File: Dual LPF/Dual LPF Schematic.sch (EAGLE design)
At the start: 84 parts, among them U1 TL074_, U2 TL074_, U3 TL074_

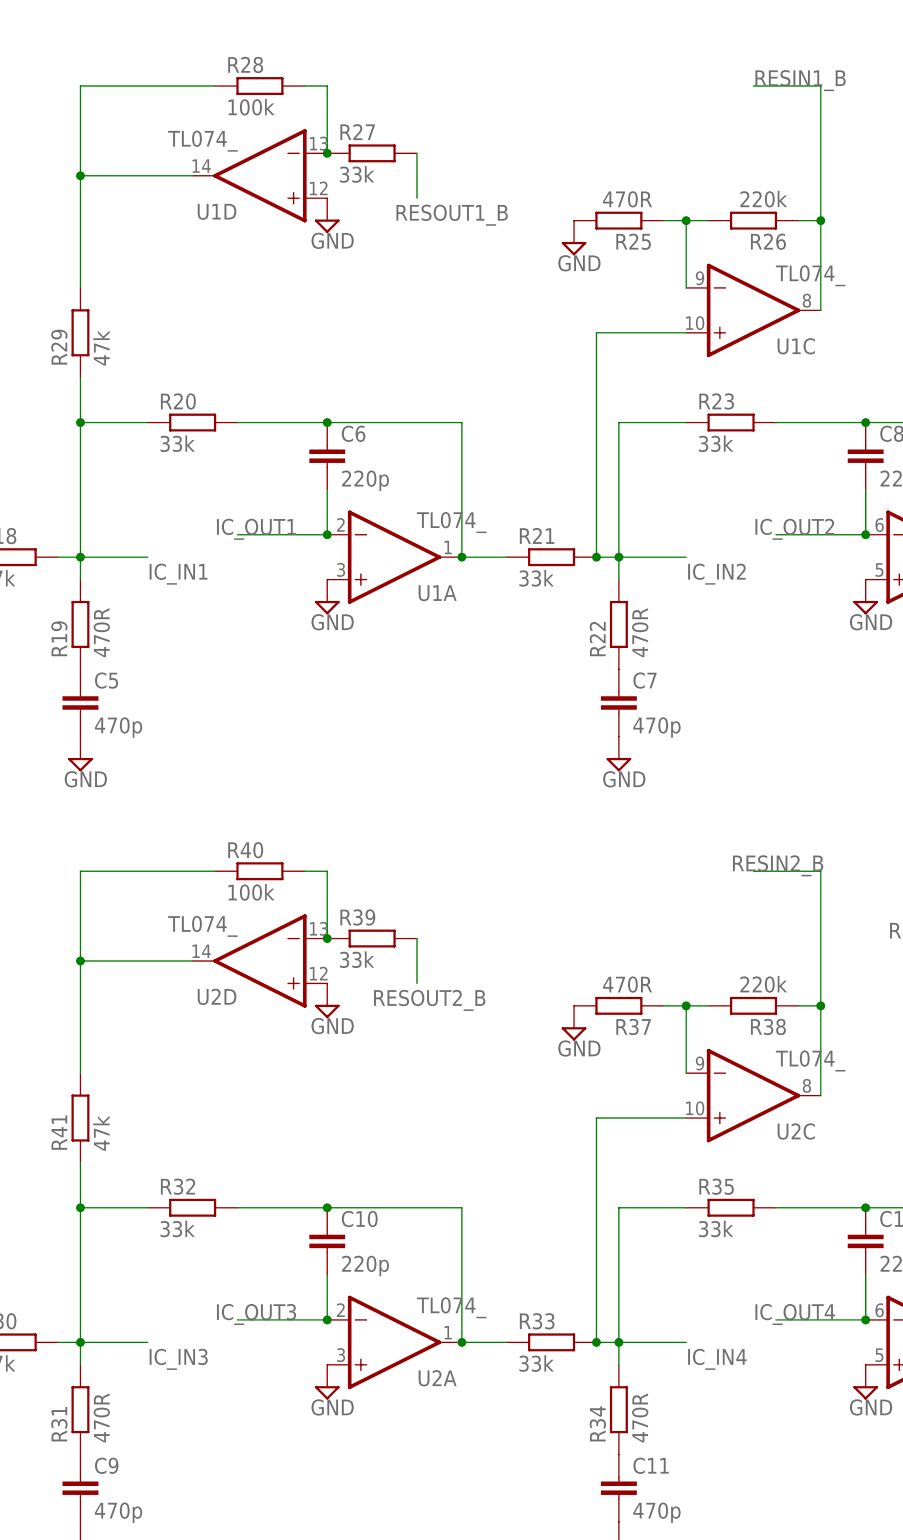
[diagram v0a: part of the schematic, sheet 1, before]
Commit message: Add files via upload
Minor resistor value change
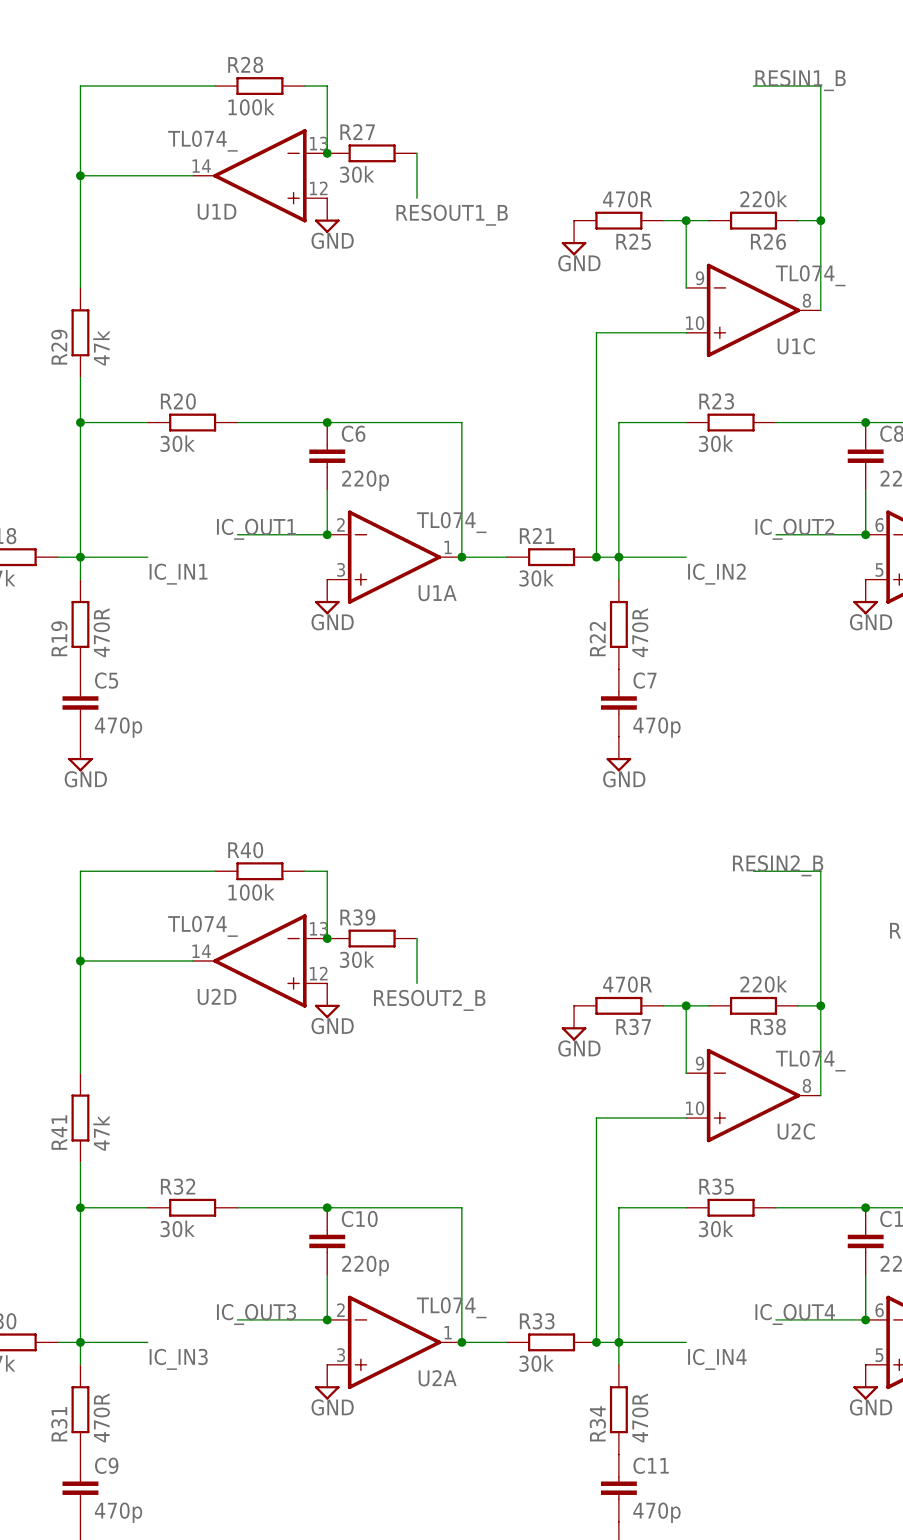
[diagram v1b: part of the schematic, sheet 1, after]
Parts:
- R20, R21, R23, R27, R32, R33, R35, R39: value 33k -> 30k
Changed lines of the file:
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@@
 <part name="SUPPLY26" library="supply2" library_urn="urn:adsk.eagle:library:372" deviceset="GND" device=""/>
 <part name="C6" library="resistor" library_urn="urn:adsk.eagle:library:348" deviceset="C-EU" device="050-024X044" package3d_urn="urn:adsk.eagle:package:26162/1" value="220p"/>
-<part name="R20" library="resistor" library_urn="urn:adsk.eagle:library:348" deviceset="R-EU_" device="0207/7" package3d_urn="urn:adsk.eagle:package:25942/1" value="33k"/>
+<part name="R20" library="resistor" library_urn="urn:adsk.eagle:library:348" deviceset="R-EU_" device="0207/7" package3d_urn="urn:adsk.eagle:package:25942/1" value="30k"/>
 <part name="SUPPLY14" library="supply2" library_urn="urn:adsk.eagle:library:372" deviceset="GND" device=""/>
-<part name="R21" library="resistor" library_urn="urn:adsk.eagle:library:348" deviceset="R-EU_" device="0207/7" package3d_urn="urn:adsk.eagle:package:25942/1" value="33k"/>
+<part name="R21" library="resistor" library_urn="urn:adsk.eagle:library:348" deviceset="R-EU_" device="0207/7" package3d_urn="urn:adsk.eagle:package:25942/1" value="30k"/>
 <part name="C7" library="resistor" library_urn="urn:adsk.eagle:library:348" deviceset="C-EU" device="050-024X044" package3d_urn="urn:adsk.eagle:package:26162/1" value="470p"/>
 <part name="R22" library="resistor" library_urn="urn:adsk.eagle:library:348" deviceset="R-EU_" device="0207/7" package3d_urn="urn:adsk.eagle:package:25942/1" value="470R"/>
 <part name="SUPPLY20" library="supply2" library_urn="urn:adsk.eagle:library:372" deviceset="GND" device=""/>
 <part name="C8" library="resistor" library_urn="urn:adsk.eagle:library:348" deviceset="C-EU" device="050-024X044" package3d_urn="urn:adsk.eagle:package:26162/1" value="220p"/>
-<part name="R23" library="resistor" library_urn="urn:adsk.eagle:library:348" deviceset="R-EU_" device="0207/7" package3d_urn="urn:adsk.eagle:package:25942/1" value="33k"/>
+<part name="R23" library="resistor" library_urn="urn:adsk.eagle:library:348" deviceset="R-EU_" device="0207/7" package3d_urn="urn:adsk.eagle:package:25942/1" value="30k"/>
 <part name="SUPPLY27" library="supply2" library_urn="urn:adsk.eagle:library:372" deviceset="GND" device=""/>
 <part name="R24" library="resistor" library_urn="urn:adsk.eagle:library:348" deviceset="R-EU_" device="0207/7" package3d_urn="urn:adsk.eagle:package:25942/1" value="1k"/>
@@
 <part name="R25" library="resistor" library_urn="urn:adsk.eagle:library:348" deviceset="R-EU_" device="0207/7" package3d_urn="urn:adsk.eagle:package:25942/1" value="470R"/>
 <part name="R26" library="resistor" library_urn="urn:adsk.eagle:library:348" deviceset="R-EU_" device="0207/7" package3d_urn="urn:adsk.eagle:package:25942/1" value="220k"/>
-<part name="R27" library="resistor" library_urn="urn:adsk.eagle:library:348" deviceset="R-EU_" device="0207/7" package3d_urn="urn:adsk.eagle:package:25942/1" value="33k"/>
+<part name="R27" library="resistor" library_urn="urn:adsk.eagle:library:348" deviceset="R-EU_" device="0207/7" package3d_urn="urn:adsk.eagle:package:25942/1" value="30k"/>
 <part name="R28" library="resistor" library_urn="urn:adsk.eagle:library:348" deviceset="R-EU_" device="0207/7" package3d_urn="urn:adsk.eagle:package:25942/1" value="100k"/>
 <part name="R29" library="resistor" library_urn="urn:adsk.eagle:library:348" deviceset="R-EU_" device="0207/7" package3d_urn="urn:adsk.eagle:package:25942/1" value="47k"/>
@@
 <part name="SUPPLY32" library="supply2" library_urn="urn:adsk.eagle:library:372" deviceset="GND" device=""/>
 <part name="C10" library="resistor" library_urn="urn:adsk.eagle:library:348" deviceset="C-EU" device="050-024X044" package3d_urn="urn:adsk.eagle:package:26162/1" value="220p"/>
-<part name="R32" library="resistor" library_urn="urn:adsk.eagle:library:348" deviceset="R-EU_" device="0207/7" package3d_urn="urn:adsk.eagle:package:25942/1" value="33k"/>
+<part name="R32" library="resistor" library_urn="urn:adsk.eagle:library:348" deviceset="R-EU_" device="0207/7" package3d_urn="urn:adsk.eagle:package:25942/1" value="30k"/>
 <part name="SUPPLY33" library="supply2" library_urn="urn:adsk.eagle:library:372" deviceset="GND" device=""/>
-<part name="R33" library="resistor" library_urn="urn:adsk.eagle:library:348" deviceset="R-EU_" device="0207/7" package3d_urn="urn:adsk.eagle:package:25942/1" value="33k"/>
+<part name="R33" library="resistor" library_urn="urn:adsk.eagle:library:348" deviceset="R-EU_" device="0207/7" package3d_urn="urn:adsk.eagle:package:25942/1" value="30k"/>
 <part name="C11" library="resistor" library_urn="urn:adsk.eagle:library:348" deviceset="C-EU" device="050-024X044" package3d_urn="urn:adsk.eagle:package:26162/1" value="470p"/>
 <part name="R34" library="resistor" library_urn="urn:adsk.eagle:library:348" deviceset="R-EU_" device="0207/7" package3d_urn="urn:adsk.eagle:package:25942/1" value="470R"/>
 <part name="SUPPLY34" library="supply2" library_urn="urn:adsk.eagle:library:372" deviceset="GND" device=""/>
 <part name="C12" library="resistor" library_urn="urn:adsk.eagle:library:348" deviceset="C-EU" device="050-024X044" package3d_urn="urn:adsk.eagle:package:26162/1" value="220p"/>
-<part name="R35" library="resistor" library_urn="urn:adsk.eagle:library:348" deviceset="R-EU_" device="0207/7" package3d_urn="urn:adsk.eagle:package:25942/1" value="33k"/>
+<part name="R35" library="resistor" library_urn="urn:adsk.eagle:library:348" deviceset="R-EU_" device="0207/7" package3d_urn="urn:adsk.eagle:package:25942/1" value="30k"/>
 <part name="SUPPLY35" library="supply2" library_urn="urn:adsk.eagle:library:372" deviceset="GND" device=""/>
 <part name="R36" library="resistor" library_urn="urn:adsk.eagle:library:348" deviceset="R-EU_" device="0207/7" package3d_urn="urn:adsk.eagle:package:25942/1" value="1k"/>
@@
 <part name="R37" library="resistor" library_urn="urn:adsk.eagle:library:348" deviceset="R-EU_" device="0207/7" package3d_urn="urn:adsk.eagle:package:25942/1" value="470R"/>
 <part name="R38" library="resistor" library_urn="urn:adsk.eagle:library:348" deviceset="R-EU_" device="0207/7" package3d_urn="urn:adsk.eagle:package:25942/1" value="220k"/>
-<part name="R39" library="resistor" library_urn="urn:adsk.eagle:library:348" deviceset="R-EU_" device="0207/7" package3d_urn="urn:adsk.eagle:package:25942/1" value="33k"/>
+<part name="R39" library="resistor" library_urn="urn:adsk.eagle:library:348" deviceset="R-EU_" device="0207/7" package3d_urn="urn:adsk.eagle:package:25942/1" value="30k"/>
 <part name="R40" library="resistor" library_urn="urn:adsk.eagle:library:348" deviceset="R-EU_" device="0207/7" package3d_urn="urn:adsk.eagle:package:25942/1" value="100k"/>
 <part name="R41" library="resistor" library_urn="urn:adsk.eagle:library:348" deviceset="R-EU_" device="0207/7" package3d_urn="urn:adsk.eagle:package:25942/1" value="47k"/>
